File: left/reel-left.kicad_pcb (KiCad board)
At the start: 2 copper layers, 146.2 x 93.3 mm, 49 parts, among them J1 Conn_01x02, SW1 SW_Push, SW10 SW_Push, SW11 SW_Push, SW12 SW_Push, SW13 SW_Push, SW14 SW_Push, SW15 SW_Push, SW16 SW_Push, SW17 SW_Push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

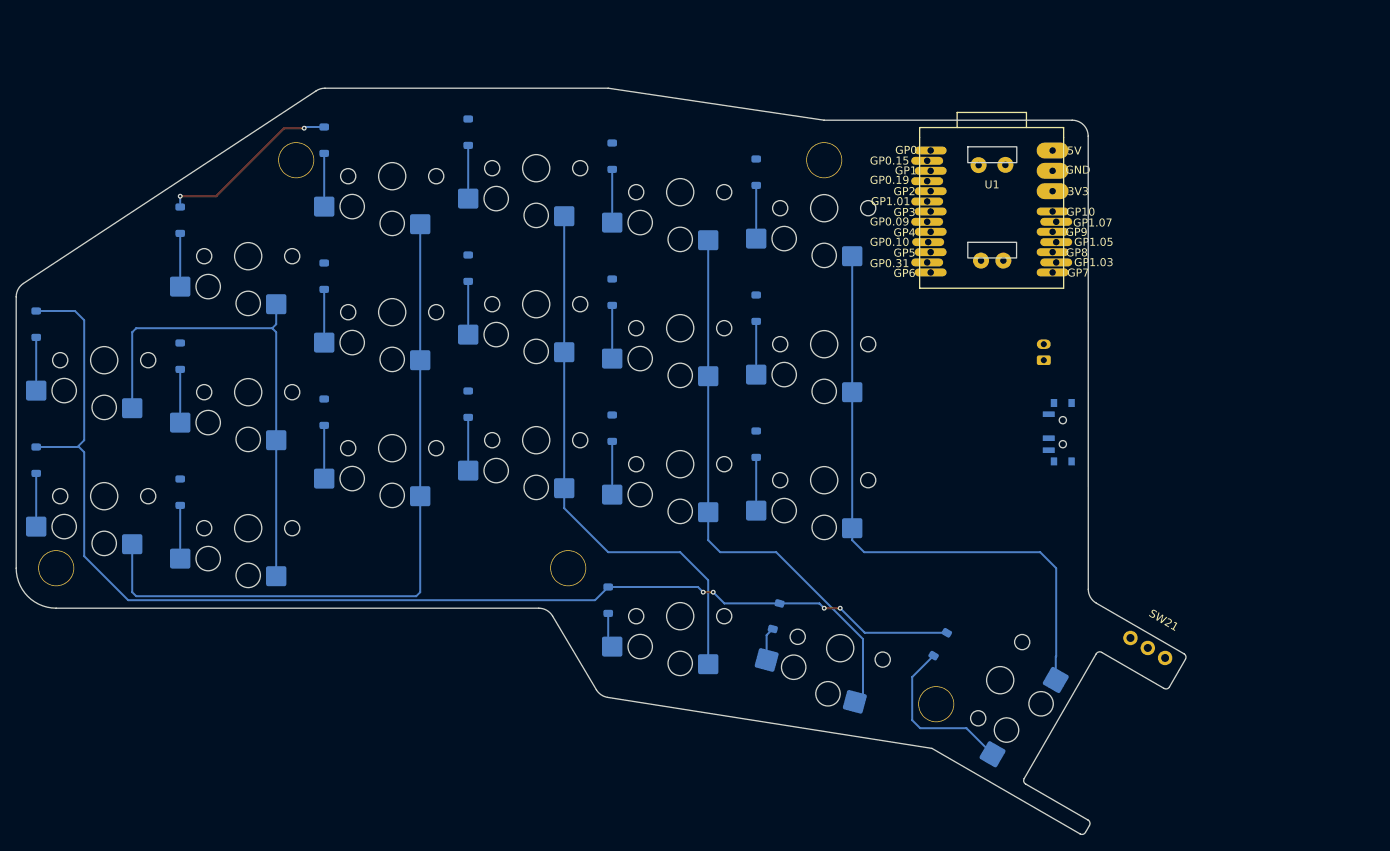
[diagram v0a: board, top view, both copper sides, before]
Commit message: Update left PCB routing
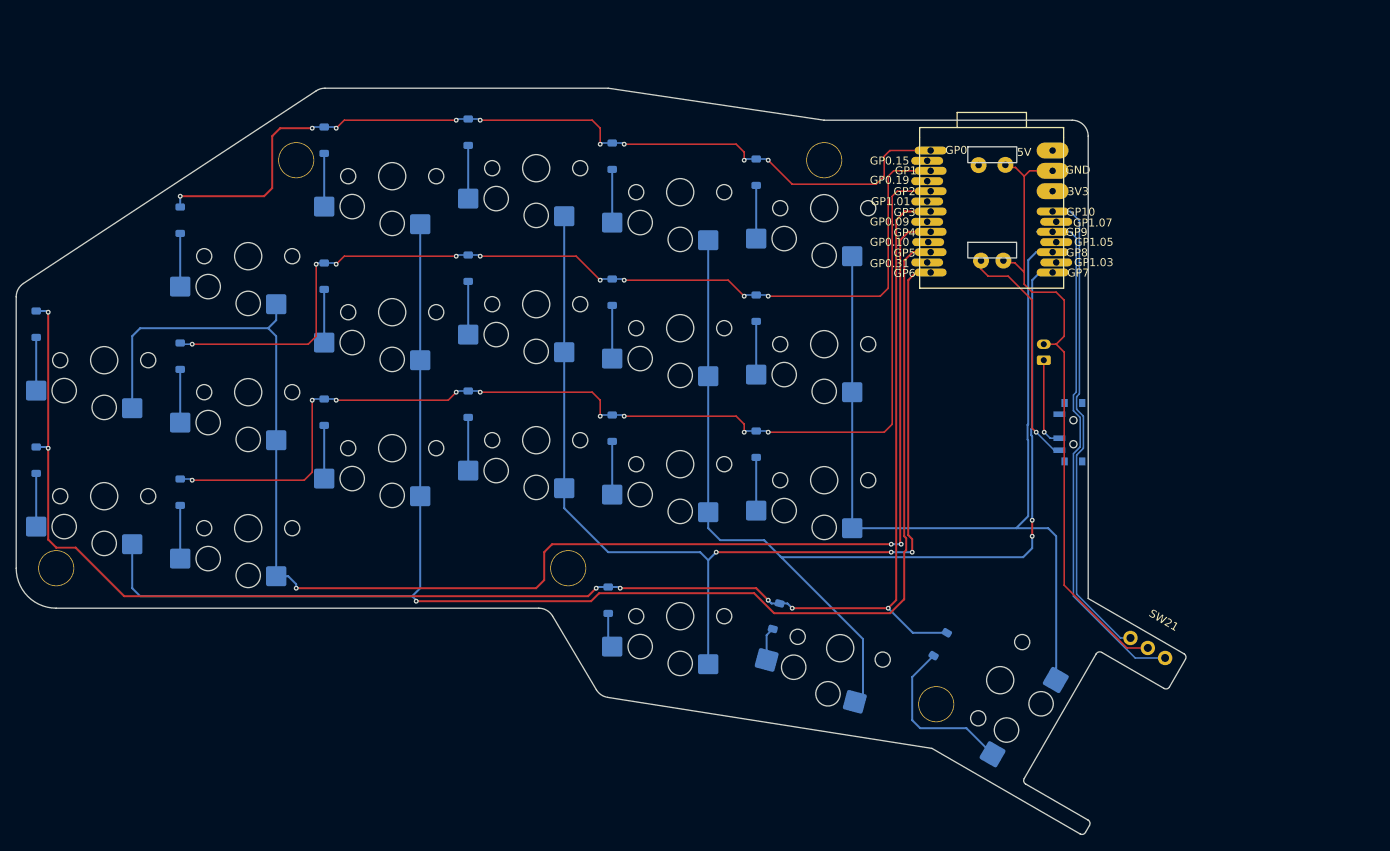
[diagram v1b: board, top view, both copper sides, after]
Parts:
- moved SW22 1.32 mm to (181.8, 105.0)
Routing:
- net Row2: track 0.00 -> 137.4 mm, vias 0 -> 9
- net Col0: track 61.6 -> 186.9 mm, vias 0 -> 3
- net Row1: track 0.00 -> 121.0 mm, vias 0 -> 9
- net Col1: track 88.4 -> 198.1 mm, vias 0 -> 1
- net Row0: track 22.9 -> 112.2 mm, vias 2 -> 9
- net GND: track 0.00 -> 82.6 mm
- net Col3: track 70.7 -> 138.4 mm, vias 0 -> 2
- net RotB: track 0.00 -> 65.6 mm
- net Col2: track 68.7 -> 133.5 mm, vias 0 -> 3
- net RotA: track 0.00 -> 60.4 mm
- net Row3: track 155.1 -> 203.3 mm, vias 4 -> 7
- net Col4: track 76.4 -> 115.6 mm
- net VBAT_SW: track 0.00 -> 29.3 mm, vias 0 -> 1
- net Net-(J1-Pin_1): track 0.00 -> 11.8 mm, vias 0 -> 1
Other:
- outline, holes or cut-outs redrawn

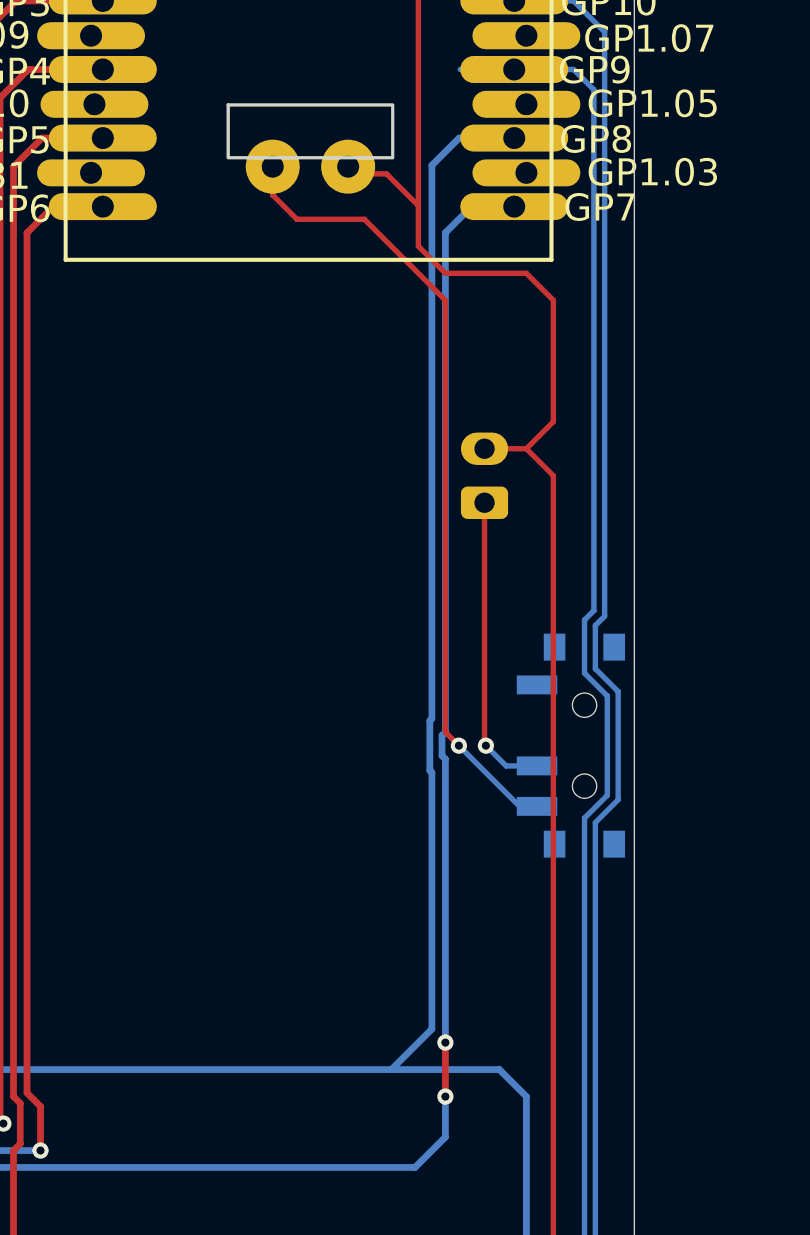
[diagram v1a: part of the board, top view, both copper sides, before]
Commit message: Update left PCB layout
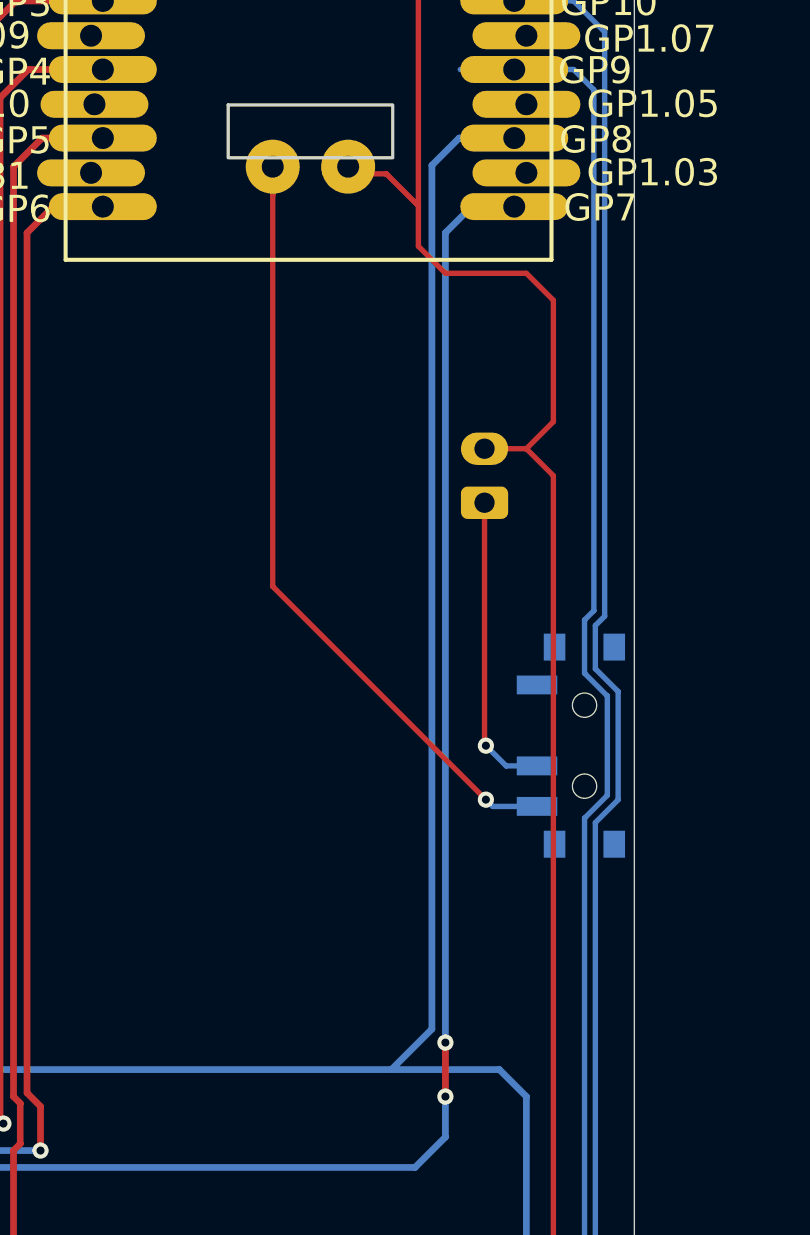
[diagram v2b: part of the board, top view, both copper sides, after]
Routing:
- net VBAT_SW: track 29.3 -> 30.1 mm
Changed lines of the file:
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@@
 	)
 	(segment
-		(start 176.425 105.925)
-		(end 176.5 106)
+		(start 176.5 83.5)
+		(end 176.5 115.5)
 		(width 0.25)
 		(layer "B.Cu")
@@
 	)
 	(segment
-		(start 176.5 83.5)
-		(end 176.5 104)
-		(width 0.25)
-		(layer "B.Cu")
-		(net "Col4")
-	)
-	(segment
-		(start 176.425 104.075)
-		(end 176.425 105.925)
-		(width 0.25)
-		(layer "B.Cu")
-		(net "Col4")
-	)
-	(segment
 		(start 180 134.5)
 		(end 180 118)
@@
 	)
 	(segment
+		(start 176.5 115.5)
+		(end 175 117)
+		(width 0.25)
+		(layer "B.Cu")
+		(net "Col4")
+	)
+	(segment
 		(start 175 117)
 		(end 154.5 117)
@@
 	)
 	(segment
+		(start 154.5 100)
+		(end 154.5 117)
+		(width 0.25)
+		(layer "B.Cu")
+		(net "Col4")
+	)
+	(segment
+		(start 179 117)
+		(end 175 117)
+		(width 0.25)
+		(layer "B.Cu")
+		(net "Col4")
+	)
+	(segment
+		(start 179.946152 134.553848)
+		(end 180 134.5)
+		(width 0.25)
+		(layer "B.Cu")
+		(net "Col4")
+	)
+	(segment
 		(start 179.55 82.49)
 		(end 177.51 82.49)
@@
 	)
 	(segment
-		(start 175 117)
-		(end 176.5 115.5)
-		(width 0.25)
-		(layer "B.Cu")
-		(net "Col4")
-	)
-	(segment
-		(start 154.5 100)
-		(end 154.5 117)
-		(width 0.25)
-		(layer "B.Cu")
-		(net "Col4")
-	)
-	(segment
-		(start 179 117)
-		(end 175 117)
-		(width 0.25)
-		(layer "B.Cu")
-		(net "Col4")
-	)
-	(segment
-		(start 179.946152 134.553848)
-		(end 180 134.5)
-		(width 0.25)
-		(layer "B.Cu")
-		(net "Col4")
-	)
-	(segment
-		(start 176.5 104)
-		(end 176.425 104.075)
-		(width 0.25)
-		(layer "B.Cu")
-		(net "Col4")
-	)
-	(segment
 		(start 179.946152 135.968911)
 		(end 179.946152 134.553848)
@@
 	)
 	(segment
-		(start 176.5 115.5)
-		(end 176.5 106)
-		(width 0.25)
-		(layer "B.Cu")
-		(net "Col4")
-	)
-	(segment
 		(start 142.5 108.15)
 		(end 142.5 114.8)
@@
 	)
 	(segment
-		(start 177 105.5)
-		(end 176.875 105.375)
-		(width 0.25)
-		(layer "B.Cu")
-		(net "Col3")
-	)
-	(segment
-		(start 177 86)
-		(end 177.97 85.03)
-		(width 0.25)
-		(layer "B.Cu")
-		(net "Col3")
-	)
-	(segment
 		(start 143.5 118.5)
 		(end 145.5 120.5)
@@
 	)
 	(segment
+		(start 177.97 85.03)
+		(end 177 86)
+		(width 0.25)
+		(layer "B.Cu")
+		(net "Col3")
+	)
+	(segment
+		(start 177 86)
+		(end 177 116)
+		(width 0.25)
+		(layer "B.Cu")
+		(net "Col3")
+	)
+	(segment
 		(start 177 119.5)
 		(end 177 118)
@@
 	)
 	(segment
-		(start 177 116)
-		(end 177 105.5)
-		(width 0.25)
-		(layer "B.Cu")
-		(net "Col3")
-	)
-	(segment
 		(start 136.5 117)
 		(end 138 118.5)
@@
 	)
 	(segment
+		(start 179.55 85.03)
+		(end 177.97 85.03)
+		(width 0.25)
+		(layer "B.Cu")
+		(net "Col3")
+	)
+	(segment
 		(start 145.5 120.5)
 		(end 155.848447 130.848447)
@@
 	)
 	(segment
-		(start 177.97 85.03)
-		(end 179.55 85.03)
-		(width 0.25)
-		(layer "B.Cu")
-		(net "Col3")
-	)
-	(segment
-		(start 176.875 104.625)
-		(end 177 104.5)
-		(width 0.25)
-		(layer "B.Cu")
-		(net "Col3")
-	)
-	(segment
 		(start 145.5 120.5)
 		(end 145.625 120.625)
@@
 	)
 	(segment
-		(start 177 104.5)
-		(end 177 86)
-		(width 0.25)
-		(layer "B.Cu")
-		(net "Col3")
-	)
-	(segment
-		(start 176.875 105.375)
-		(end 176.875 104.625)
-		(width 0.25)
-		(layer "B.Cu")
-		(net "Col3")
-	)
-	(segment
 		(start 143.806118 133.470556)
 		(end 143.806118 130.360607)
@@
 	)
 	(segment
-		(start 174 85.5)
-		(end 171.5 85.5)
+		(start 178.5 107)
+		(end 170.603 99.103)
 		(width 0.2)
 		(layer "F.Cu")
@@
 	)
 	(segment
-		(start 171.5 85.5)
-		(end 170.603 84.603)
+		(start 170.603 99.103)
+		(end 170.603 83.5702)
 		(width 0.2)
 		(layer "F.Cu")
 		(net "VBAT_SW")
 	)
-	(segment
-		(start 177.5 105)
-		(end 177 104.5)
-		(width 0.2)
-		(layer "F.Cu")
-		(net "VBAT_SW")
-	)
-	(segment
-		(start 177 88.5)
-		(end 174 85.5)
-		(width 0.2)
-		(layer "F.Cu")
-		(net "VBAT_SW")
-	)
-	(segment
-		(start 177 104.5)
-		(end 177 88.5)
-		(width 0.2)
-		(layer "F.Cu")
-		(net "VBAT_SW")
-	)
-	(via
-		(at 177.5 105)
+	(via
+		(at 178.5 107)
 		(size 0.6)
 		(drill 0.3)
@@
 	)
 	(segment
-		(start 179.75 107.25)
-		(end 177.5 105)
-		(width 0.2)
-		(layer "B.Cu")
+		(start 178.75 107.25)
+		(end 178.5 107)
+		(width 0.2)
+		(layer "B.Cu")
+		(net "VBAT_SW")
+	)
+	(segment
+		(start 180.395 107.25)
+		(end 178.75 107.25)
+		(width 0.2)
+		(layer "B.Cu")

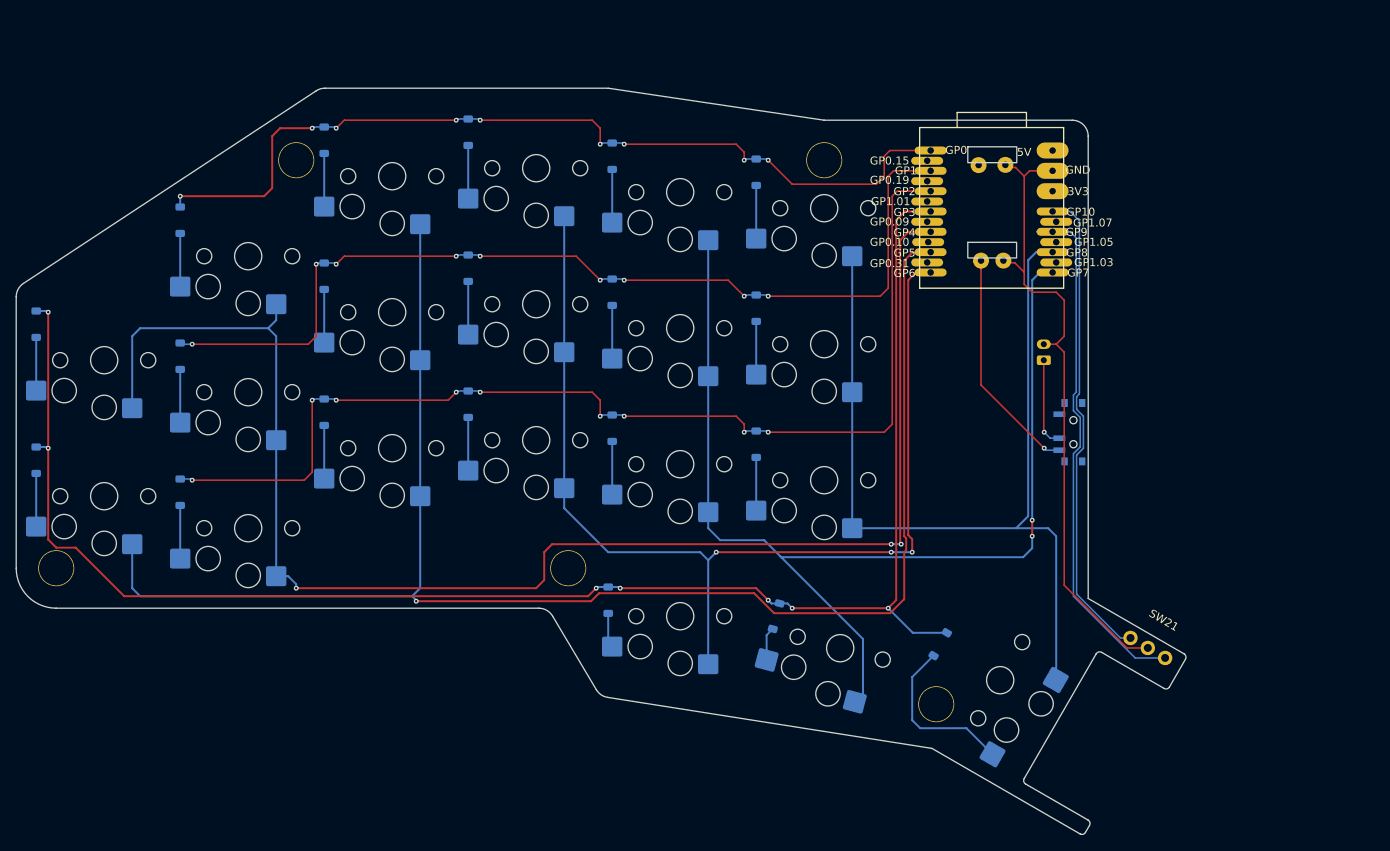
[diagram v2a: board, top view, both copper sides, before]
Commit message: Update left and right PCB layouts
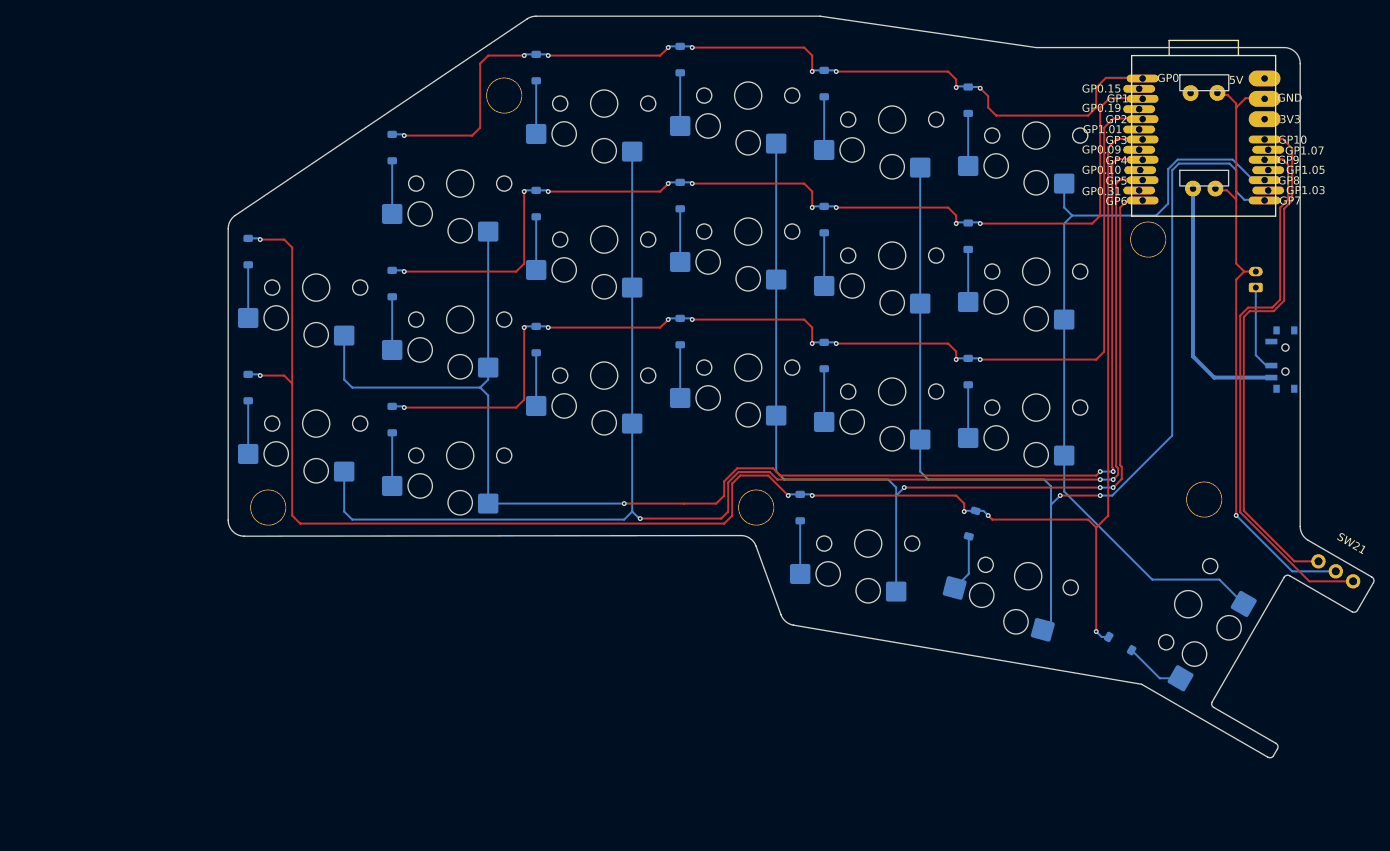
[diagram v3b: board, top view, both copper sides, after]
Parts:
- moved Ref** 42.1 mm to (198.5, 113.4)
- moved Ref** 41.7 mm to (191.5, 80.9)
- moved D1 28.0 mm to (97.0, 69.4)
- moved D11 28.0 mm to (97.0, 103.4)
- moved D12 28.0 mm to (115.0, 93.4)
- moved D13 28.0 mm to (133.0, 92.4)
- moved D14 28.0 mm to (151.0, 95.4)
- moved D15 28.0 mm to (169.0, 97.4)
- moved D16 28.0 mm to (79.0, 82.4)
- moved D17 28.0 mm to (79.0, 99.4)
- moved D2 28.0 mm to (115.0, 59.4)
- moved D3 28.0 mm to (133.0, 58.4)
- moved D4 28.0 mm to (151.0, 61.4)
- moved D6 28.0 mm to (97.0, 86.4)
- moved D7 28.0 mm to (115.0, 76.4)
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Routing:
- net Row3: track 203.3 -> 222.4 mm
- net Col4: track 115.5 -> 98.1 mm
- net Net-(D20-A): track 21.0 -> 7.57 mm
- net RotA: track 60.4 -> 65.4 mm
- net Col1: track 198.1 -> 193.1 mm, vias 1 -> 3
- net Col0: track 186.9 -> 182.0 mm
- net GND: track 82.6 -> 79.0 mm, vias 0 -> 1
- net RotB: track 65.6 -> 68.6 mm
- net Net-(D19-A): track 4.19 -> 7.19 mm
- net Col3: track 138.3 -> 141.1 mm
- net Col2: track 133.5 -> 136.1 mm
- net Net-(D18-A): track 4.92 -> 6.65 mm
- net VBAT_SW: track 30.1 -> 31.5 mm, vias 1 -> 0
- net Row1: track 121.0 -> 122.4 mm
- net Net-(J1-Pin_1): track 11.8 -> 10.9 mm, vias 1 -> 0
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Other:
- board size 146.2 x 93.3 mm -> 143.2 x 92.7 mm
